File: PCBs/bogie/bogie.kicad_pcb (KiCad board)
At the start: 2 copper layers, 56.5 x 78 mm, 2 parts

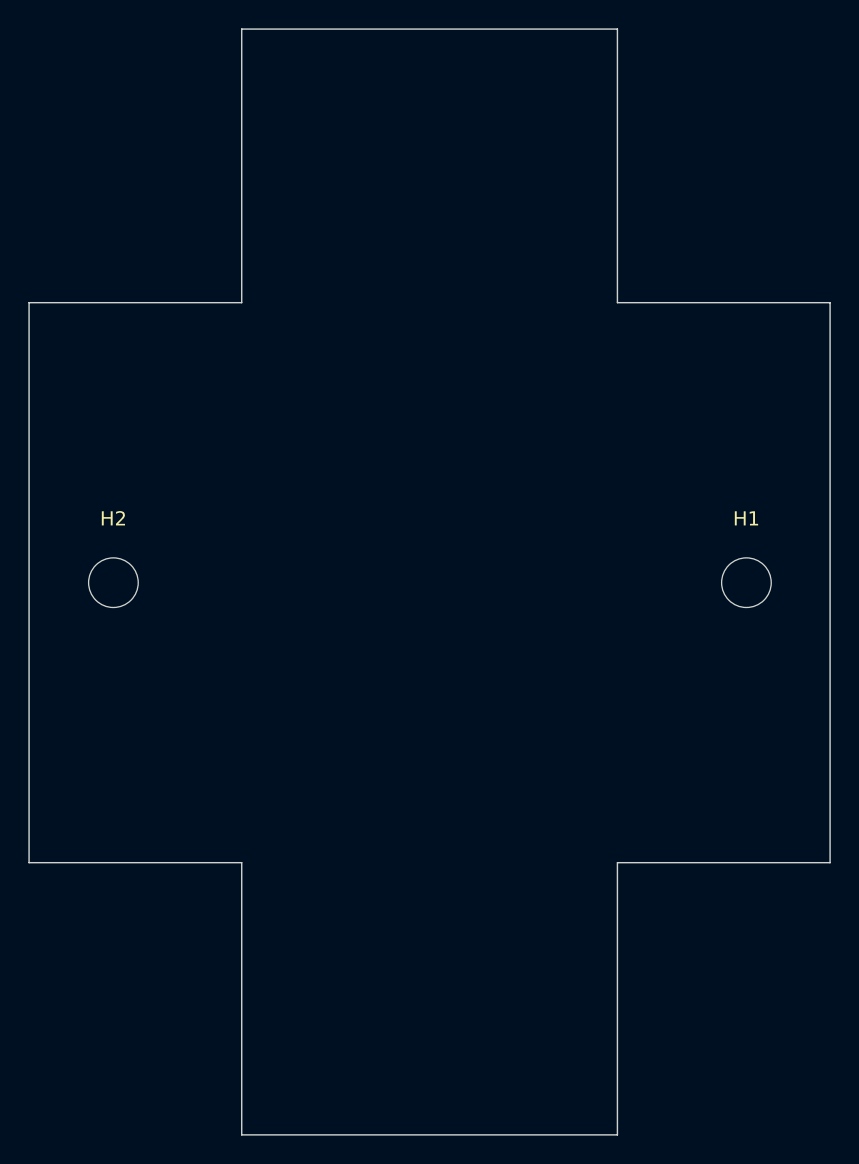
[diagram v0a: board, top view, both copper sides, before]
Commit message: Torso, bogie and rail complete. Next up: revise hand and IMU board in conjunction
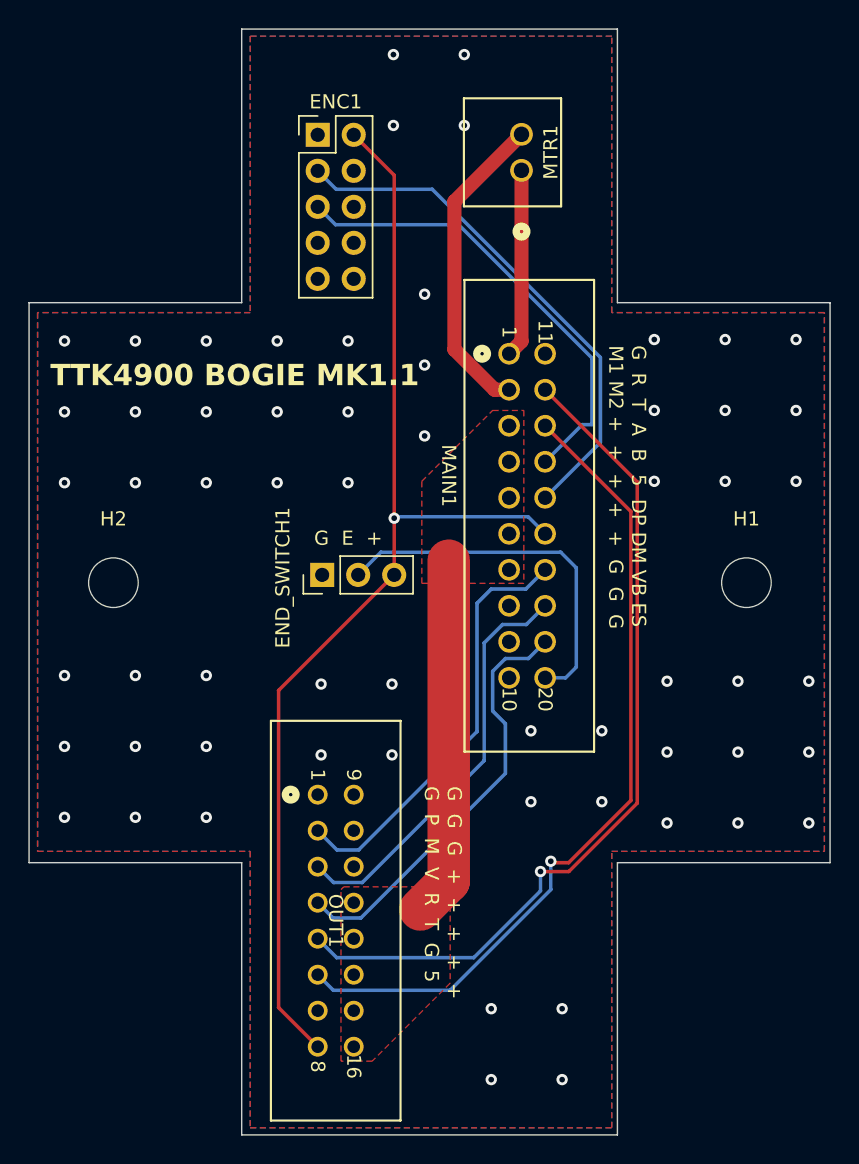
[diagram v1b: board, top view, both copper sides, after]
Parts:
- added ENC1: Conn_02x05_Odd_Even, Connector_PinHeader_2.54mm:PinHeader_2x05_P2.54mm_Vertical, F.Cu at (94.3, 28.0)
- added END_SWITCH1: Conn_01x03, Connector_PinHeader_2.54mm:PinHeader_1x03_P2.54mm_Vertical, F.Cu at (94.6, 59.0)
- added MAIN1: Conn_02x10_Top_Bottom, 1761681-7:1761681-7_TYC, F.Cu at (107.8, 43.4)
- added MTR1: Conn_01x02, 70543-0001:70543-0001_MOL, F.Cu at (108.6, 30.5)
- added OUT1: Conn_02x08_Top_Bottom, 2-1761603-6:2-1761603-6_TYC, F.Cu at (94.3, 74.5)
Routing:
- net +5V: track 0.00 -> 81.2 mm, vias 0 -> 1
- net /UART_RX: track 0.00 -> 60.3 mm, vias 0 -> 1
- net /UART_TX: track 0.00 -> 58.3 mm, vias 0 -> 1
- net /ENC1A: track 0.00 -> 36.9 mm
- net /ENC1B: track 0.00 -> 32.8 mm
- net /DP_OUT: track 0.00 -> 30.1 mm
- net /VB_OUT: track 0.00 -> 30.0 mm
- net /DM_OUT: track 0.00 -> 29.5 mm
- net /END_SWITCH: track 0.00 -> 26.0 mm
- net +48V: track 0.00 -> 25.4 mm
- net /MTR1_OUT: track 0.00 -> 22.2 mm
- net /MTR1_IN: track 0.00 -> 13.3 mm
- net GND: vias 0 -> 61
- added copper zone on F.Cu, net +48V
- added copper zone on B.Cu, net GND
- added copper zone on F.Cu, net GND
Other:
- board text added: "G E +"
- board text added: "G G G + + + + + G P M V R T G 5"
- board text added: "G R T A B 5 DP DM VB ES M1 M2 + + + + + G G G"
- board text added: "KRISTIAN BLOM"
- board text added: "TTK4900 BOGIE MK1.1"
